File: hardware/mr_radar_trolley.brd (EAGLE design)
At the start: 100 x 80 mm, 42 parts, among them IC1 AD711RN, IC2 REG1117, IC3 REG1117, IC4 LM2940, U1 FT232RL-BASICSSOP

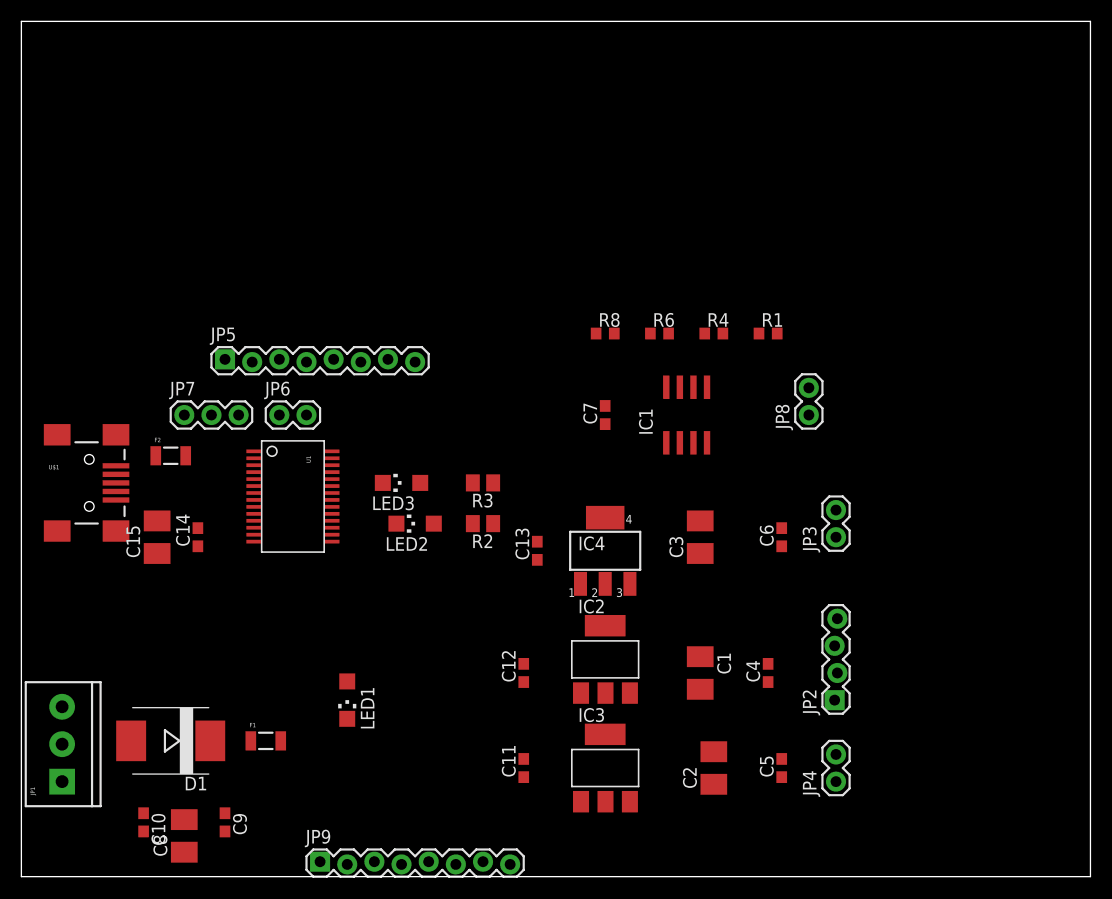
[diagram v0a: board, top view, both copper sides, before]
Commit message: finished component placement draft on mr_radar_trolley
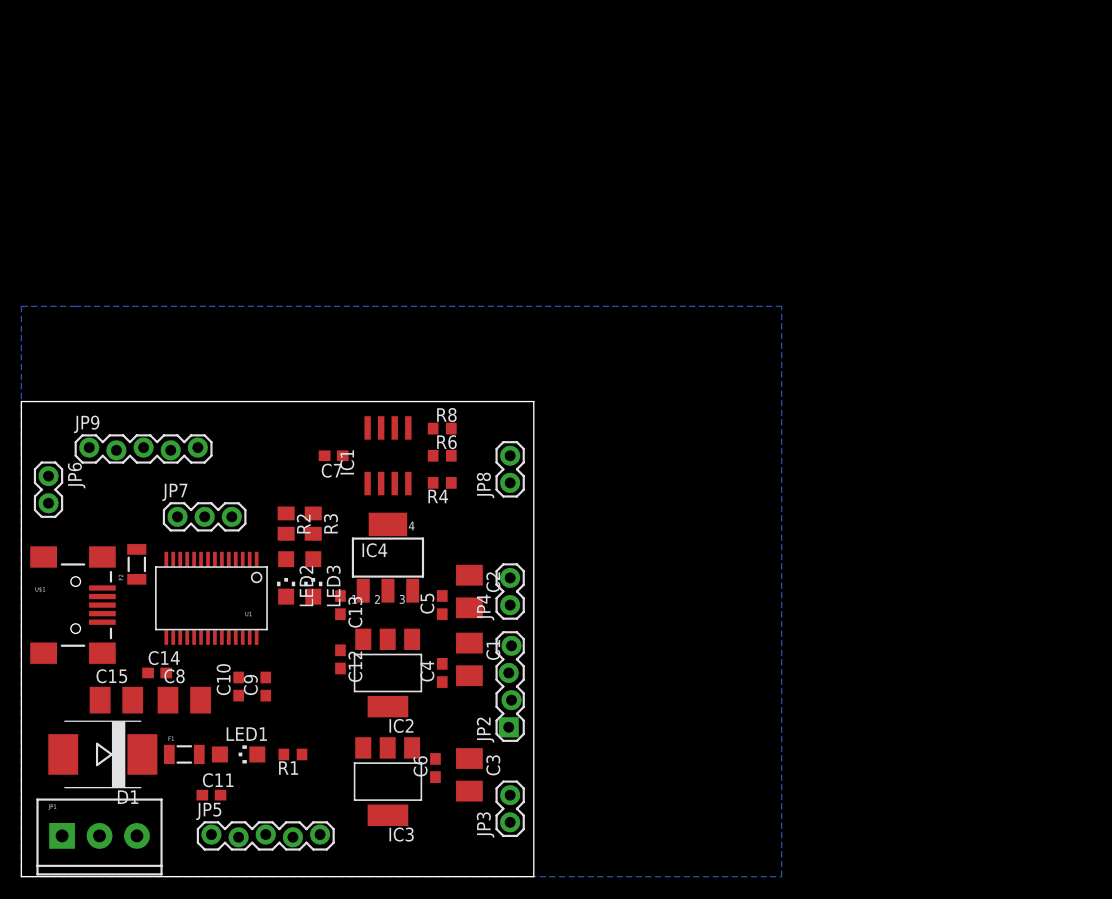
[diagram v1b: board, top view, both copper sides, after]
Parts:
- JP5, JP9: device SparkFun-Connectors:1X08_LOCK -> SparkFun-Connectors:1X05_LOCK
- moved R1 59.4 mm to (25.4, 11.4), turned to 180 degrees
- moved JP5 44.5 mm to (17.8, 3.81)
- moved JP9 44.3 mm to (6.35, 40.0)
- moved JP3 40.5 mm to (45.7, 5.08)
- moved C6 38.9 mm to (38.7, 10.2)
- moved C5 35.2 mm to (39.4, 25.4)
- moved JP4 34.7 mm to (45.7, 25.4)
- moved C3 31.0 mm to (41.9, 9.53), turned to 270 degrees
- moved JP2 30.6 mm to (45.7, 14.0)
- moved C4 30.5 mm to (39.4, 19.1)
- moved C11 29.3 mm to (17.8, 7.62), turned to 0 degrees
- moved R4 29.0 mm to (39.4, 36.8), turned to 180 degrees
- moved JP8 28.7 mm to (45.7, 36.8)
- moved C2 28.2 mm to (41.9, 26.7), turned to 270 degrees
- moved IC1 28.2 mm to (34.3, 39.4)
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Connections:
- net +3V3: now also C3.+
- net GND: no longer JP5.6, JP5.7, JP5.8, JP9.6, JP9.7, JP9.8
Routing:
- added copper zone on layer 16, net GND
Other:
- board size 100 x 80 mm -> 47.9 x 44.4 mm

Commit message: finished mr_radar_trolley layout
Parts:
- moved JP6 21.9 mm to (24.1, 41.3), turned to 180 degrees
- moved C15 17.8 mm to (7.62, 34.3), turned to 270 degrees
- moved C14 15.4 mm to (10.8, 34.3), turned to 90 degrees
- moved C1 2.54 mm to (41.9, 17.8), turned to 90 degrees
- moved JP7 2.01 mm to (16.5, 34.3)
- moved C12 1.27 mm to (29.8, 19.1)
- moved C3 1.27 mm to (41.9, 10.8)
- moved JP9 1.27 mm to (6.35, 41.3)
- moved C6 0.90 mm to (39.4, 10.8)
- moved C13 0.64 mm to (29.8, 26.0)
- moved C4 0.64 mm to (39.4, 18.4), turned to 270 degrees
- turned R6 to 180 degrees
- turned R8 to 180 degrees
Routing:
- net V+: track 0.00 -> 48.8 mm
- net +10V: track 0.00 -> 38.9 mm
- net GND: track 0.00 -> 27.4 mm, vias 0 -> 33
- net +5V: track 0.00 -> 22.8 mm
- net +3V3: track 0.00 -> 18.3 mm
- net N$10: track 0.00 -> 17.5 mm
- net N$7: track 0.00 -> 15.1 mm, vias 0 -> 2
- net N$17: track 0.00 -> 14.7 mm
- net N$9: track 0.00 -> 13.8 mm
- net N$8: track 0.00 -> 12.5 mm
- net N$11: track 0.00 -> 11.8 mm
- net N$2: track 0.00 -> 10.1 mm
- net N$16: track 0.00 -> 9.85 mm
- net N$12: track 0.00 -> 9.83 mm
- net N$5: track 0.00 -> 9.10 mm
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- added copper zone on layer 1, net GND
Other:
- board text added: "10v"
- board text added: "16V max"
- board text added: "3.3v"
- board text added: "5v"
- board text added: "gnd"
- board text added: "in"
- board text added: "mr_radar_trolley kl1xf r0"
- board text added: "out"
- board text added: "rxd"
- board text added: "txd"
- board text added: "vin"

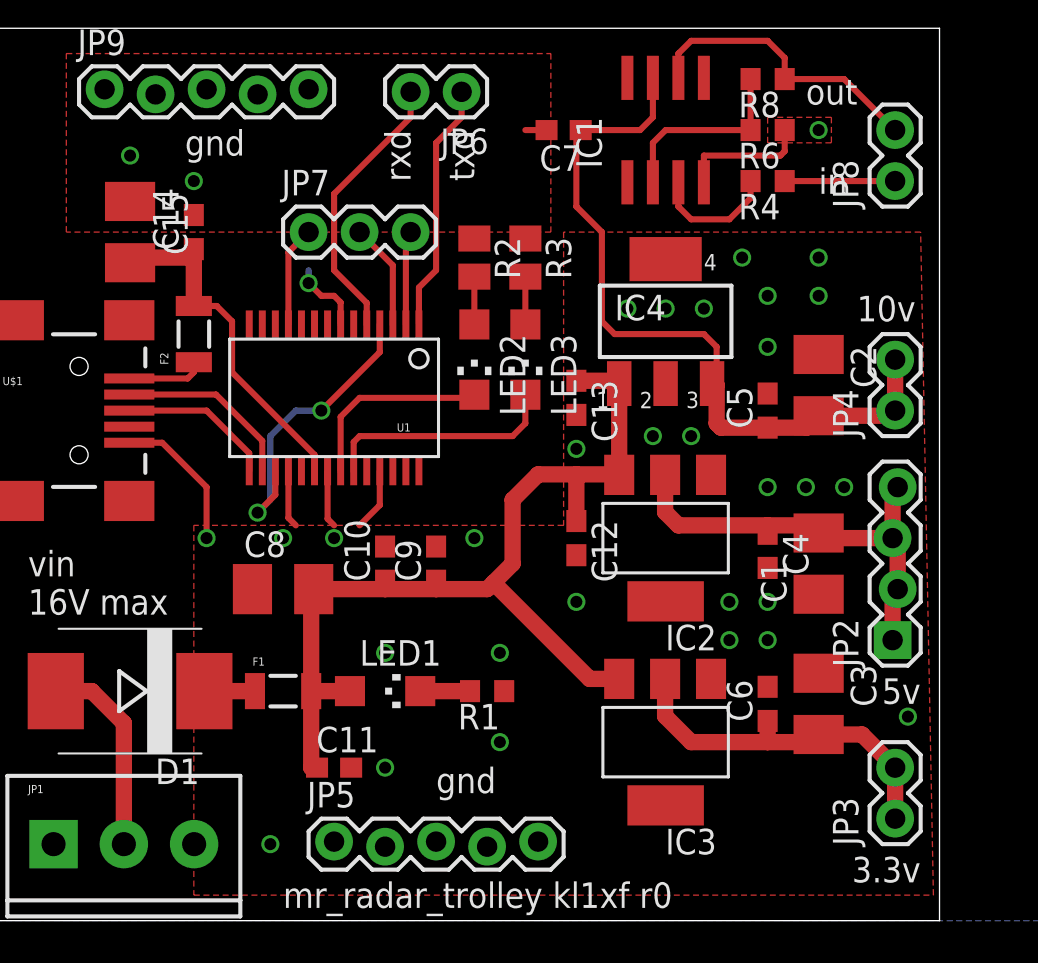
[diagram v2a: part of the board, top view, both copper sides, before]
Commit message: fixes to ft232rl layout and schematic, cleanup of silkscreen layer, sent for manufacturing
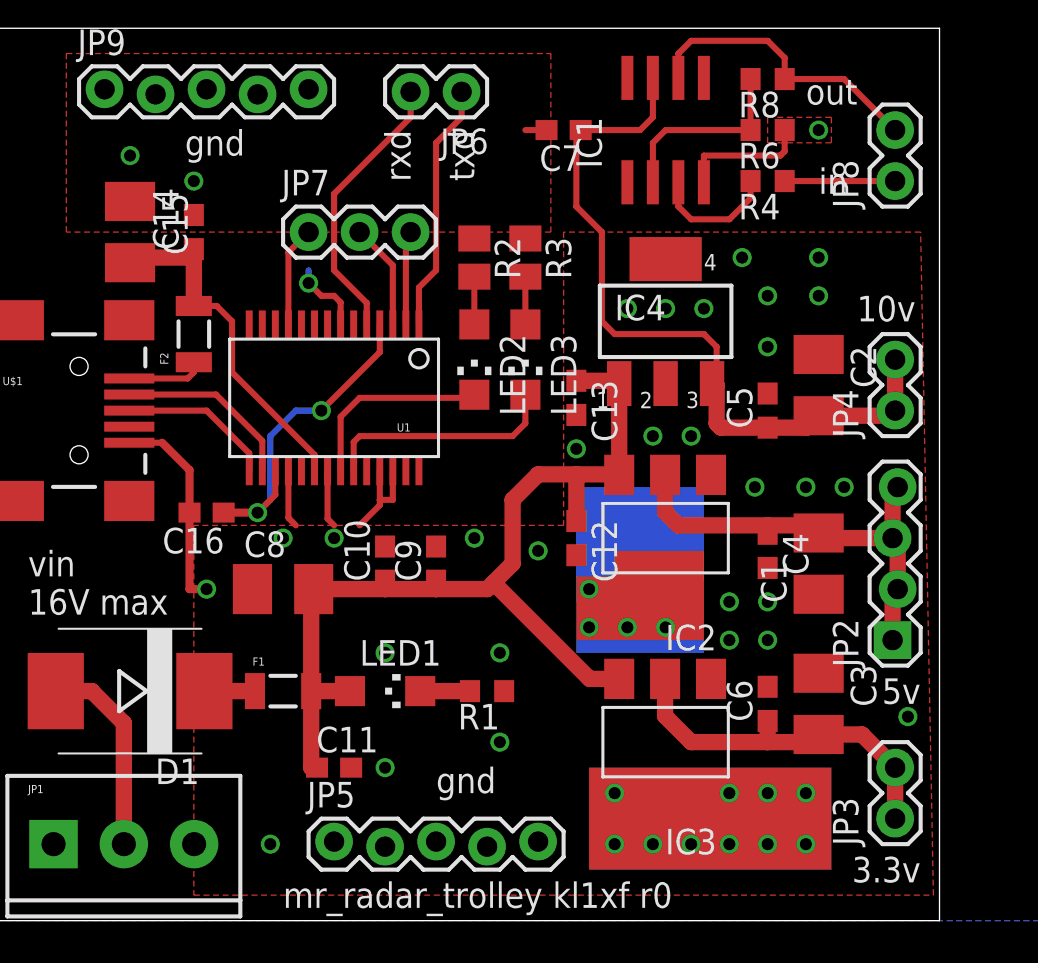
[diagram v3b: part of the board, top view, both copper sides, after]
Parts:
- added C16: 100nF, resistor:C0603
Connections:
- net GND: now also C16.2, U1.26
- net N$7: now also C16.1
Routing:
- net GND: track 27.4 -> 32.5 mm
- net N$7: track 15.1 -> 16.8 mm
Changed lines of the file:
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@@
 <layer number="116" name="Patch_BOT" color="9" fill="4" visible="no" active="yes"/>
 <layer number="121" name="_tsilk" color="7" fill="1" visible="yes" active="yes"/>
-<layer number="122" name="_bsilk" color="7" fill="1" visible="no" active="yes"/>
+<layer number="122" name="_bsilk" color="7" fill="1" visible="yes" active="yes"/>
 <layer number="125" name="_tNames" color="7" fill="1" visible="no" active="yes"/>
 <layer number="144" name="Drill_legend" color="7" fill="1" visible="no" active="yes"/>
@@
 <text x="2.54" y="17.145" size="1.27" layer="121" font="vector" ratio="10">vin</text>
 <text x="15.24" y="0.635" size="1.27" layer="121" font="vector" ratio="10">mr_radar_trolley kl1xf r0</text>
+<rectangle x1="31.75" y1="13.97" x2="36.195" y2="18.415" layer="1"/>
+<rectangle x1="29.845" y1="13.97" x2="34.925" y2="17.145" layer="1"/>
+<rectangle x1="30.48" y1="2.54" x2="42.545" y2="7.62" layer="1"/>
+<rectangle x1="30.48" y1="2.54" x2="42.545" y2="7.62" layer="16"/>
+<rectangle x1="29.845" y1="15.875" x2="36.195" y2="19.685" layer="16"/>
+<rectangle x1="29.845" y1="13.335" x2="36.195" y2="17.78" layer="16"/>
+<rectangle x1="29.845" y1="15.875" x2="36.195" y2="21.59" layer="16"/>
 </plain>
 <attributes>
@@
 Einstellungen hier und speichern die Design Rules unter
 einem neuen Namen ab.</description>
-<description language="en">&lt;b&gt;EAGLE Design Rules&lt;/b&gt;
+<description language="en">&lt;b&gt;Laen's PCB Order Design Rules&lt;/b&gt;
 &lt;p&gt;
-The default Design Rules have been set to cover
-a wide range of applications. Your particular design
-may have different requirements, so please make the
-necessary adjustments and save your customized
-design rules under a new name.</description>
-<description language="zh">&lt;b&gt;Seeed Studio EAGLE Design Rules&lt;/b&gt;
-</description>
+Please make sure your boards conform to these design rules.</description>
 <param name="layerSetup" value="(1*16)"/>
-<param name="mtCopper" value="0.035mm 0.035mm 0.035mm 0.035mm 0.035mm 0.035mm 0.035mm 0.035mm 0.035mm 0.035mm 0.035mm 0.035mm 0.035mm 0.035mm 0.035mm 0.035mm"/>
-<param name="mtIsolate" value="1.5mm 0.15mm 0.2mm 0.15mm 0.2mm 0.15mm 0.2mm 0.15mm 0.2mm 0.15mm 0.2mm 0.15mm 0.2mm 0.15mm 0.2mm"/>
+<param name="mtCopper" value="0.0356mm 0.0356mm 0.0356mm 0.0356mm 0.0356mm 0.0356mm 0.0356mm 0.0356mm 0.0356mm 0.0356mm 0.0356mm 0.0356mm 0.0356mm 0.0356mm 0.0356mm 0.0356mm"/>
+<param name="mtIsolate" value="1.5011mm 0.1499mm 0.2007mm 0.1499mm 0.2007mm 0.1499mm 0.2007mm 0.1499mm 0.2007mm 0.1499mm 0.2007mm 0.1499mm 0.2007mm 0.1499mm 0.2007mm"/>
 <param name="mdWireWire" value="6mil"/>
 <param name="mdWirePad" value="6mil"/>
@@
 <param name="mdPadVia" value="6mil"/>
 <param name="mdViaVia" value="6mil"/>
-<param name="mdSmdPad" value="0mil"/>
-<param name="mdSmdVia" value="0mil"/>
-<param name="mdSmdSmd" value="0mil"/>
+<param name="mdSmdPad" value="6mil"/>
+<param name="mdSmdVia" value="6mil"/>
+<param name="mdSmdSmd" value="6mil"/>
 <param name="mdViaViaSameLayer" value="8mil"/>
 <param name="mnLayersViaInSmd" value="2"/>
-<param name="mdCopperDimension" value="10mil"/>
-<param name="mdDrill" value="10mil"/>
+<param name="mdCopperDimension" value="15mil"/>
+<param name="mdDrill" value="6mil"/>
 <param name="mdSmdStop" value="0mil"/>
 <param name="msWidth" value="6mil"/>
-<param name="msDrill" value="12mil"/>
-<param name="msMicroVia" value="12mil"/>
+<param name="msDrill" value="13mil"/>
+<param name="msMicroVia" value="13mil"/>
 <param name="msBlindViaRatio" value="0.5"/>
 <param name="rvPadTop" value="0.25"/>
@@
 <param name="rvMicroViaOuter" value="0.25"/>
 <param name="rvMicroViaInner" value="0.25"/>
-<param name="rlMinPadTop" value="10mil"/>
+<param name="rlMinPadTop" value="7mil"/>
 <param name="rlMaxPadTop" value="20mil"/>
-<param name="rlMinPadInner" value="10mil"/>
+<param name="rlMinPadInner" value="7mil"/>
 <param name="rlMaxPadInner" value="20mil"/>
-<param name="rlMinPadBottom" value="10mil"/>
+<param name="rlMinPadBottom" value="7mil"/>
 <param name="rlMaxPadBottom" value="20mil"/>
-<param name="rlMinViaOuter" value="6mil"/>
+<param name="rlMinViaOuter" value="7mil"/>
 <param name="rlMaxViaOuter" value="20mil"/>
-<param name="rlMinViaInner" value="6mil"/>
+<param name="rlMinViaInner" value="7mil"/>
 <param name="rlMaxViaInner" value="20mil"/>
 <param name="rlMinMicroViaOuter" value="4mil"/>
@@
 <param name="psTop" value="-1"/>
 <param name="psBottom" value="-1"/>
-<param name="psFirst" value="0"/>
+<param name="psFirst" value="-1"/>
 <param name="psElongationLong" value="100"/>
 <param name="psElongationOffset" value="100"/>
 <param name="mvStopFrame" value="1"/>
 <param name="mvCreamFrame" value="0"/>
-<param name="mlMinStopFrame" value="2mil"/>
-<param name="mlMaxStopFrame" value="2mil"/>
+<param name="mlMinStopFrame" value="4mil"/>
+<param name="mlMaxStopFrame" value="4mil"/>
 <param name="mlMinCreamFrame" value="0mil"/>
 <param name="mlMaxCreamFrame" value="0mil"/>
-<param name="mlViaStopLimit" value="100mil"/>
+<param name="mlViaStopLimit" value="0mil"/>
 <param name="srRoundness" value="0"/>
 <param name="srMinRoundness" value="0mil"/>
@@
 <param name="checkAngle" value="0"/>
 <param name="checkFont" value="1"/>
-<param name="checkRestrict" value="0"/>
+<param name="checkRestrict" value="1"/>
 <param name="useDiameter" value="13"/>
 <param name="maxErrors" value="50"/>
@@
 <element name="JP5" library="SparkFun-Connectors" package="1X05_LOCK" value="" x="17.78" y="3.81"/>
 <element name="JP9" library="SparkFun-Connectors" package="1X05_LOCK" value="" x="6.35" y="41.275"/>
+<element name="C16" library="resistor" package="C0603" value="100nF" x="11.43" y="20.32" rot="R180"/>
 </elements>
 <signals>
@@
 <vertex x="29.21" y="19.685"/>
 </polygon>
-<via x="29.845" y="15.875" extent="1-16" drill="0.6"/>
+<via x="27.94" y="18.415" extent="1-16" drill="0.6"/>
 <via x="37.465" y="15.875" extent="1-16" drill="0.6"/>
 <via x="39.37" y="15.875" extent="1-16" drill="0.6"/>
 <via x="39.37" y="13.97" extent="1-16" drill="0.6"/>
 <via x="37.465" y="13.97" extent="1-16" drill="0.6"/>
-<via x="39.37" y="21.59" extent="1-16" drill="0.6"/>
+<via x="38.735" y="21.59" extent="1-16" drill="0.6"/>
 <via x="41.275" y="21.59" extent="1-16" drill="0.6"/>
 <via x="43.18" y="21.59" extent="1-16" drill="0.6"/>
@@
 <via x="15.24" y="19.05" extent="1-16" drill="0.6"/>
 <wire x1="7.58" y1="23.8" x2="9.22" y2="23.8" width="0.3048" layer="1"/>
-<wire x1="9.22" y1="23.8" x2="11.43" y2="21.59" width="0.3048" layer="1"/>
-<wire x1="11.43" y1="21.59" x2="11.43" y2="19.05" width="0.3048" layer="1"/>
-<via x="11.43" y="19.05" extent="1-16" drill="0.6"/>
+<via x="11.43" y="16.51" extent="1-16" drill="0.6"/>
 <via x="10.795" y="36.83" extent="1-16" drill="0.6"/>
 <via x="7.62" y="38.1" extent="1-16" drill="0.6"/>
-<wire x1="20.055" y1="22.379" x2="20.055" y2="20.69" width="0.3048" layer="1"/>
+<wire x1="20.055" y1="22.379" x2="20.055" y2="20.955" width="0.3048" layer="1"/>
+<wire x1="20.055" y1="20.955" x2="20.055" y2="20.69" width="0.3048" layer="1"/>
 <wire x1="20.055" y1="20.69" x2="19.05" y2="19.685" width="0.3048" layer="1"/>
 <wire x1="17.455" y1="22.379" x2="17.455" y2="20.01" width="0.3048" layer="1"/>
@@
 <via x="38.1" y="33.02" extent="1-16" drill="0.6"/>
 <via x="41.91" y="33.02" extent="1-16" drill="0.6"/>
+<contactref element="C16" pad="2"/>
+<contactref element="U1" pad="26"/>
+<wire x1="9.22" y1="23.8" x2="10.58" y2="22.44" width="0.4064" layer="1"/>
+<wire x1="10.58" y1="22.44" x2="10.58" y2="20.32" width="0.4064" layer="1"/>
+<wire x1="10.58" y1="20.32" x2="10.58" y2="16.51" width="0.4064" layer="1"/>
+<wire x1="10.58" y1="16.51" x2="11.43" y2="16.51" width="0.4064" layer="1"/>
+<wire x1="20.705" y1="22.379" x2="20.705" y2="20.955" width="0.3048" layer="1"/>
+<wire x1="20.705" y1="20.955" x2="20.055" y2="20.955" width="0.3048" layer="1"/>
 </signal>
 <signal name="+3V3">
@@
 <wire x1="13.97" y1="20.32" x2="14.855" y2="21.205" width="0.3048" layer="1"/>
 <wire x1="14.855" y1="21.205" x2="14.855" y2="22.379" width="0.3048" layer="1"/>
+<contactref element="C16" pad="1"/>
+<wire x1="12.28" y1="20.32" x2="13.97" y2="20.32" width="0.4064" layer="1"/>
 </signal>
 <signal name="N$10">
@@
 <wire x1="38.52" y1="36.83" x2="38.52" y2="35.98" width="0.3048" layer="1"/>
 </signal>
+<signal name="N$20">
+<via x="31.75" y="6.35" extent="1-16" drill="0.6"/>
+</signal>
+<signal name="N$21">
+<via x="31.75" y="3.81" extent="1-16" drill="0.6"/>
+</signal>
+<signal name="N$22">
+<via x="33.655" y="3.81" extent="1-16" drill="0.6"/>
+</signal>
+<signal name="N$23">
+<via x="35.56" y="3.81" extent="1-16" drill="0.6"/>
+</signal>
+<signal name="N$24">
+<via x="37.465" y="3.81" extent="1-16" drill="0.6"/>
+</signal>
+<signal name="N$25">
+<via x="37.465" y="6.35" extent="1-16" drill="0.6"/>
+</signal>
+<signal name="N$26">
+<via x="39.37" y="6.35" extent="1-16" drill="0.6"/>
+</signal>
+<signal name="N$27">
+<via x="41.275" y="6.35" extent="1-16" drill="0.6"/>
+</signal>
+<signal name="N$28">
+<via x="41.275" y="3.81" extent="1-16" drill="0.6"/>
+</signal>
+<signal name="N$29">
+<via x="39.37" y="3.81" extent="1-16" drill="0.6"/>
+</signal>
+<signal name="N$30">
+<via x="30.48" y="16.51" extent="1-16" drill="0.6"/>
+</signal>
+<signal name="N$31">
+<via x="30.48" y="14.605" extent="1-16" drill="0.6"/>
+</signal>
+<signal name="N$32">
+<via x="32.385" y="14.605" extent="1-16" drill="0.6"/>
+</signal>
+<signal name="N$33">
+<via x="34.29" y="14.605" extent="1-16" drill="0.6"/>
+</signal>
 </signals>
